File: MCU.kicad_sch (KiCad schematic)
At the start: 13 parts, among them U2 LPC55S28JBD100, Y1 24MHz

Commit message: LM2596 Layout oluşturuldu, USB Power switch tarafı eksik
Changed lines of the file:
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@@
   (junction (at 55.88 173.355) (diameter 0) (color 0 0 0 0)
   )
+  (wire (pts (xy 129.54 106.045) (xy 123.19 106.045))
+    (stroke (width 0) (type default) (color 0 0 0 0))
+  )
   (wire (pts (xy 279.4 23.495) (xy 279.4 57.785))
     (stroke (width 0.5) (type solid) (color 57 87 255 1))
@@
     (stroke (width 0) (type default) (color 0 0 0 0))
   )
+  (wire (pts (xy 129.54 116.205) (xy 123.19 116.205))
+    (stroke (width 0) (type default) (color 0 0 0 0))
+  )
   (wire (pts (xy 31.115 184.785) (xy 31.115 188.595))
     (stroke (width 0) (type default) (color 0 0 0 0))
@@
   )
   (wire (pts (xy 124.46 188.595) (xy 124.46 184.785))
+    (stroke (width 0) (type default) (color 0 0 0 0))
+  )
+  (wire (pts (xy 129.54 113.665) (xy 123.19 113.665))
     (stroke (width 0) (type default) (color 0 0 0 0))
   )
@@
     (effects (font (size 1.27 1.27)) (justify right bottom))
   )
-  (label "MCU_VDD" (at 123.19 116.205 0)
+  (label "MCU_VDD" (at 129.54 116.205 0)
     (effects (font (size 1.27 1.27)) (justify left bottom))
   )
@@
     (effects (font (size 1.27 1.27)) (justify left bottom))
   )
-  (label "MCU_VDDA" (at 123.19 113.665 0)
-    (effects (font (size 1.27 1.27)) (justify left bottom))
-  )
+  (label "MCU_VDDA" (at 129.54 113.665 0)
+    (effects (font (size 1.27 1.27)) (justify left bottom))
+  )

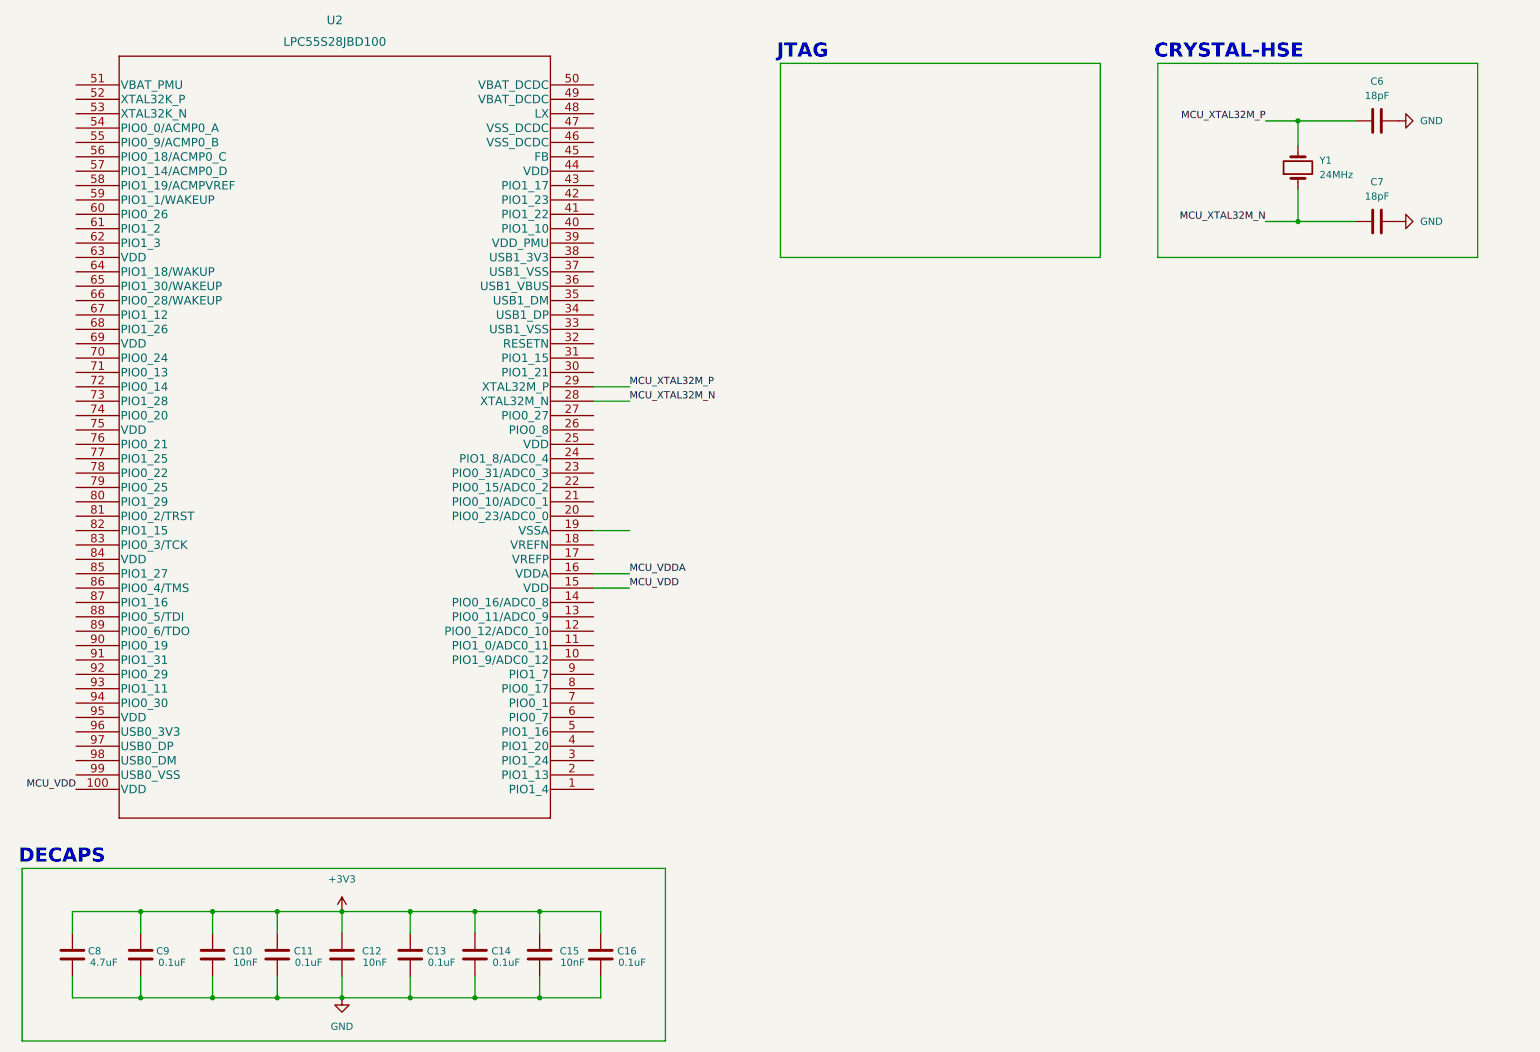
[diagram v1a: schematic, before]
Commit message: USB Current limiting devresi tamamlanacak. ADC bağlantıları yapılıyor
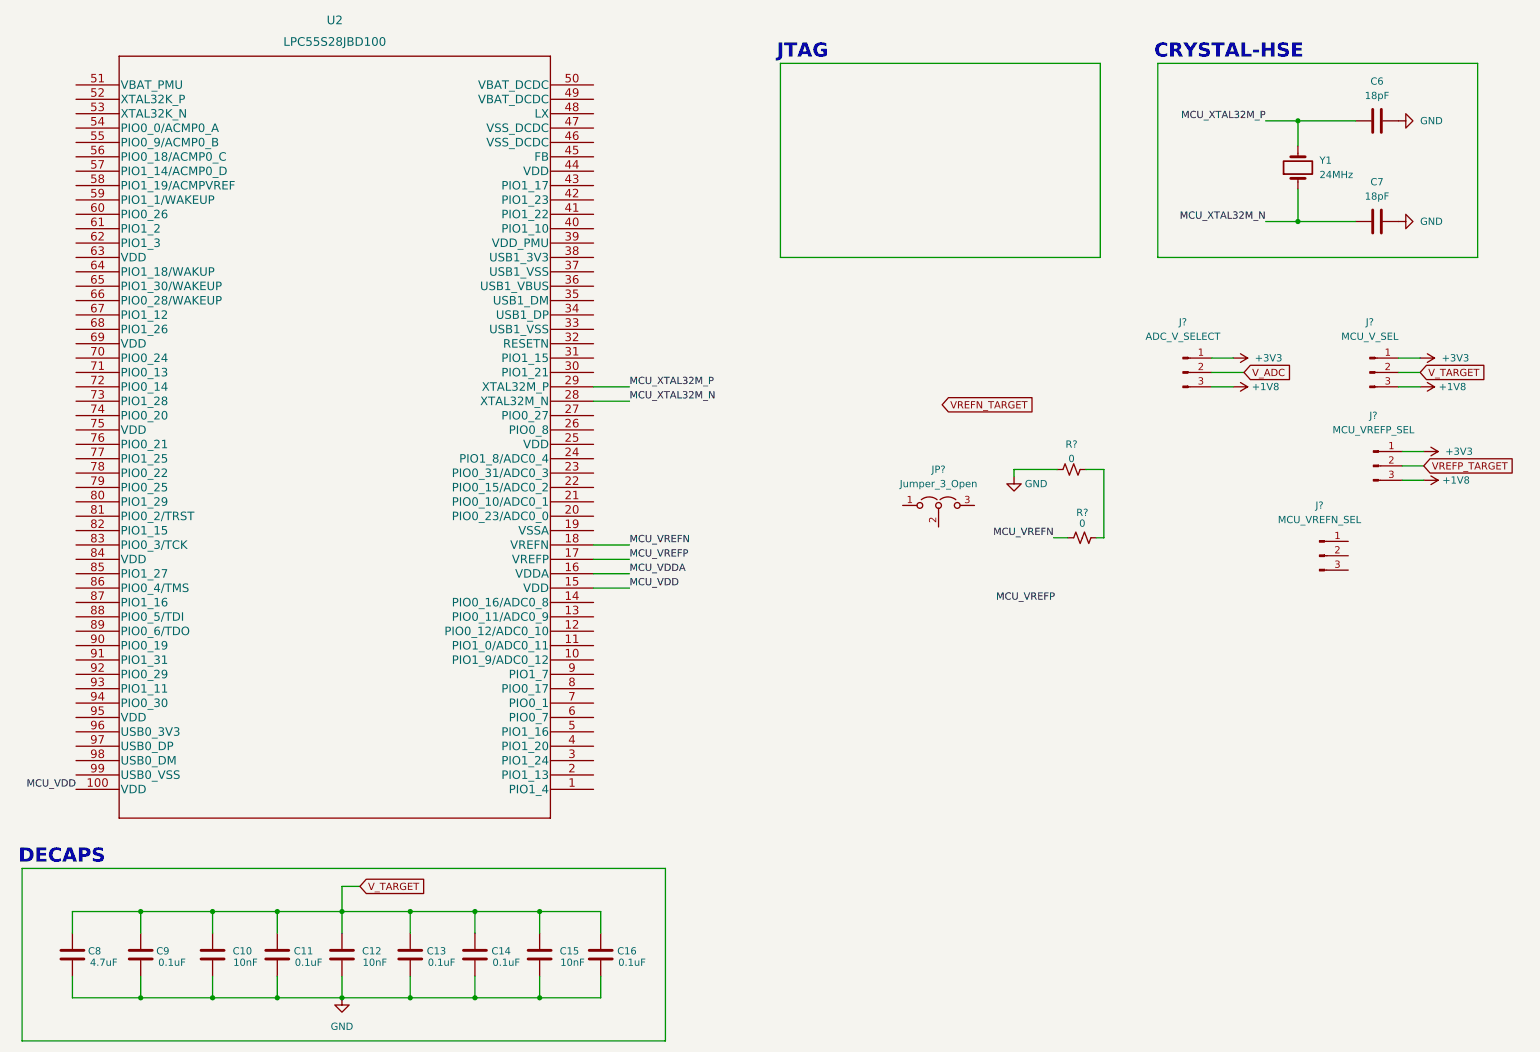
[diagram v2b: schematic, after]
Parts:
- added J?: MCU_VREFN_SEL, Connector_PinHeader_2.54mm:PinHeader_1x03_P2.54mm_Vertical, symbol Connector:Conn_01x03_Male
- added J?: MCU_V_SEL, Connector_PinHeader_2.54mm:PinHeader_1x03_P2.54mm_Vertical, symbol Connector:Conn_01x03_Male
- added J?: ADC_V_SELECT, Connector_PinHeader_2.54mm:PinHeader_1x03_P2.54mm_Vertical, symbol Connector:Conn_01x03_Male
- added J?: MCU_VREFP_SEL, Connector_PinHeader_2.54mm:PinHeader_1x03_P2.54mm_Vertical, symbol Connector:Conn_01x03_Male
- added JP?: Jumper_3_Open, Jumper:SolderJumper-3_P1.3mm_Open_Pad1.0x1.5mm_NumberLabels, symbol Jumper:Jumper_3_Open
- added R? (x2): 0, symbol Device:R_Small_US
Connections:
- net +3V3: now also J?.1 (Pin_1), J?.1 (Pin_1), J?.1 (Pin_1); no longer C10.1, C11.1, C12.1, C13.1, C14.1, C15.1, C16.1, C8.1, C9.1
- net GND: now also R?.1
- net MCU_VREFP: now reaches U2.17 (VREFP)
- net MCU_VREFN: now reaches U2.18 (VREFN)
- net MCU_VREFN: now also R?.1
- new net: R?.2, R?.2
- new net +1V8: J?.3 (Pin_3), J?.3 (Pin_3), J?.3 (Pin_3)
- new net VREFP_TARGET: J?.2 (Pin_2)
- new net V_ADC: J?.2 (Pin_2)
- new net V_TARGET: C10.1, C11.1, C12.1, C13.1, C14.1, C15.1, C16.1, C8.1, C9.1, J?.2 (Pin_2)

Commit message: MCU bölümlere ayrýldý
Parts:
- removed C6, C7: 18pF, Resistor_SMD:R_0603_1608Metric, symbol Device:C
- removed J?: MCU_VREFN_SEL, Connector_PinHeader_2.54mm:PinHeader_1x03_P2.54mm_Vertical, symbol Connector:Conn_01x03_Male
- removed J?: ADC_V_SELECT, Connector_PinHeader_2.54mm:PinHeader_1x03_P2.54mm_Vertical, symbol Connector:Conn_01x03_Male
- removed J?: MCU_VREFP_SEL, Connector_PinHeader_2.54mm:PinHeader_1x03_P2.54mm_Vertical, symbol Connector:Conn_01x03_Male
- removed JP?: Jumper_3_Open, Jumper:SolderJumper-3_P1.3mm_Open_Pad1.0x1.5mm_NumberLabels, symbol Jumper:Jumper_3_Open
- removed U2: LPC55S28JBD100, erkan-hw-lib:HLQFP100, symbol erkan-hw:LPC55S28JBD100
- removed Y1: 24MHz, Crystal:Crystal_SMD_HC49-SD, symbol Device:Crystal
- added C21, C?: 47pF, Resistor_SMD:R_0603_1608Metric, symbol Device:C
- added C22: 0.1uF, Resistor_SMD:R_0603_1608Metric, symbol Device:C
- added C23: 10nF, symbol Device:C_Small
- added J3: ADC_EXT_SUPPLY, Connector_PinHeader_2.54mm:PinHeader_1x03_P2.54mm_Vertical, symbol Connector:Conn_01x03_Male
- added R7, R8: 0, Resistor_SMD:R_0603_1608Metric, symbol Device:R_Small_US
- added U2: LPC55S28JBD100, erkan-hw-lib:HLQFP100, symbol erkan-hw:LPC55S28JBD100
- R10, R9: renamed from R?; footprint (none) -> Resistor_SMD:R_0603_1608Metric
- gave numbers to parts that had none: 1
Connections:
- net GND: now also C23.2, C?.2, J3.2 (Pin_2), U2.19 (VSSA), U2.46 (VSS_DCDC), U2.47 (VSS_DCDC)
- net VREFN_TARGET: now also R10.2, R9.2, U2.18 (VREFN)
- net VREFP_TARGET: now also C23.1, C?.1, R7.2, R8.2, U2.17 (VREFP)
- net V_TARGET: no longer C10.1, C11.1, C12.1, C13.1, C14.1, C15.1, C16.1, C8.1, C9.1
- net MCU_VREFN renamed ADC_VREFN
- net ADC_VREFN: now also J3.1 (Pin_1)
- new net: C21.2, C22.2
- new net ADC_VREFP: J3.3 (Pin_3), R8.1
- new net VDD: C10.1, C11.1, C12.1, C13.1, C14.1, C15.1, C16.1, C8.1, C9.1, U2.100 (VDD), U2.15 (VDD), U2.25 (VDD), U2.44 (VDD), U2.63 (VDD), U2.69 (VDD), U2.75 (VDD), U2.84 (VDD), U2.95 (VDD)
- new net VDDA: C21.1, C22.1, U2.16 (VDDA)
- new net VDDA_TARGET: R7.1
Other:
- note added: "MCU-ADC"
- note removed: "CRYSTAL-HSE"
- note removed: "JTAG"
- moved on the sheet: J4, R10, R9

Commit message: Reset devresi eklenecek.
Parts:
- removed C?: 47pF, Resistor_SMD:R_0603_1608Metric, symbol Device:C
- removed J4: MCU_V_SEL, Connector_PinHeader_2.54mm:PinHeader_1x03_P2.54mm_Vertical, symbol Connector:Conn_01x03_Male
- added C25, C28: 22uF, Resistor_SMD:R_0603_1608Metric, symbol Device:C
- added C26, C?: 100nF, Resistor_SMD:R_0603_1608Metric, symbol Device:C
- added C27, C? (x2): 47pF, Resistor_SMD:R_0603_1608Metric, symbol Device:C
- added C?: 2.2uF, Resistor_SMD:R_0603_1608Metric, symbol Device:C
- added J?: MCU_V_SEL, Connector_PinHeader_2.54mm:PinHeader_1x03_P2.54mm_Vertical, symbol Connector:Conn_01x03_Male
- added L2: 4.7uH, symbol Device:L_Small
- added unit 3 of U2
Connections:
- net VDD is gone; now on net V_TARGET: C10.1, C11.1, C12.1, C13.1, C14.1, C15.1, C16.1, C8.1, C9.1, U2.100 (VDD), U2.15 (VDD), U2.25 (VDD), U2.44 (VDD), U2.63 (VDD), U2.69 (VDD), U2.75 (VDD), U2.84 (VDD), U2.95 (VDD)
- net VDDA is gone; now on net V_TARGET: C21.1, C22.1, U2.16 (VDDA)
- net VDDA_TARGET is gone; now on net V_TARGET: R7.1
- net +1V8: now also J?.3 (Pin_3)
- net +3V3: now also J?.1 (Pin_1)
- net GND: now also C21.2, C22.2, U2.33 (USB1_VSS), U2.37 (USB1_VSS), U2.99 (USB0_VSS), C25.2, C26.2, C27.2, C28.2, C?.2, U2.46 (VSS_DCDC), U2.47 (VSS_DCDC); no longer U2.46 (VSS_DCDC), U2.47 (VSS_DCDC)
- net VREFP_TARGET: now also C?.1
- net V_TARGET: now also C25.1, C26.1, C27.1, J?.2 (Pin_2), U2.49 (VBAT_DCDC), U2.50 (VBAT_DCDC), U2.51 (VBAT_PMU)
- new net: C28.1, C?.1, C?.1, C?.1, C?.2, C?.2, C?.2, L2.2, U2.39 (VDD_PMU), U2.45 (FB)
- new net: L2.1, U2.48 (LX)
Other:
- note added: "1-2 3v3 2-3 1v8"
- note added: "MCU-B"
- note added: "MCU-INTERNAL DC-DC"
- moved on the sheet: C10, C11, C12, C13, C14, C15, C16, C23, C8, C9, J3, R10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

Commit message: JTAG bağlantıları tamamlanacak
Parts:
- L2: footprint (none) -> Inductor_SMD:L_0805_2012Metric
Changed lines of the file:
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@@
     (property "Reference" "L2" (id 0) (at 122.555 46.355 90))
     (property "Value" "4.7uH" (id 1) (at 122.555 50.165 90))
-    (property "Footprint" "" (id 2) (at 122.555 48.26 0)
+    (property "Footprint" "Inductor_SMD:L_0805_2012Metric" (id 2) (at 122.555 48.26 0)
       (effects (font (size 1.27 1.27)) hide)
     )
@@
   (symbol (lib_id "Device:C") (at 52.705 52.07 0) (unit 1)
     (in_bom yes) (on_board yes)
-    (property "Reference" "C26" (id 0) (at 59.055 50.8 0)
-      (effects (font (size 1.27 1.27)) (justify right))
-    )
+    (property "Reference" "C26" (id 0) (at 59.69 50.8 0)
+      (effects (font (size 1.27 1.27)) (justify right))
+    )
